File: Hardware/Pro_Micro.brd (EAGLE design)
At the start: 17.8 x 33 mm, 33 parts, among them U2 MIC5219, U3 ATMEGA32U4, X1 USB-MICROB, Y1 16MHz

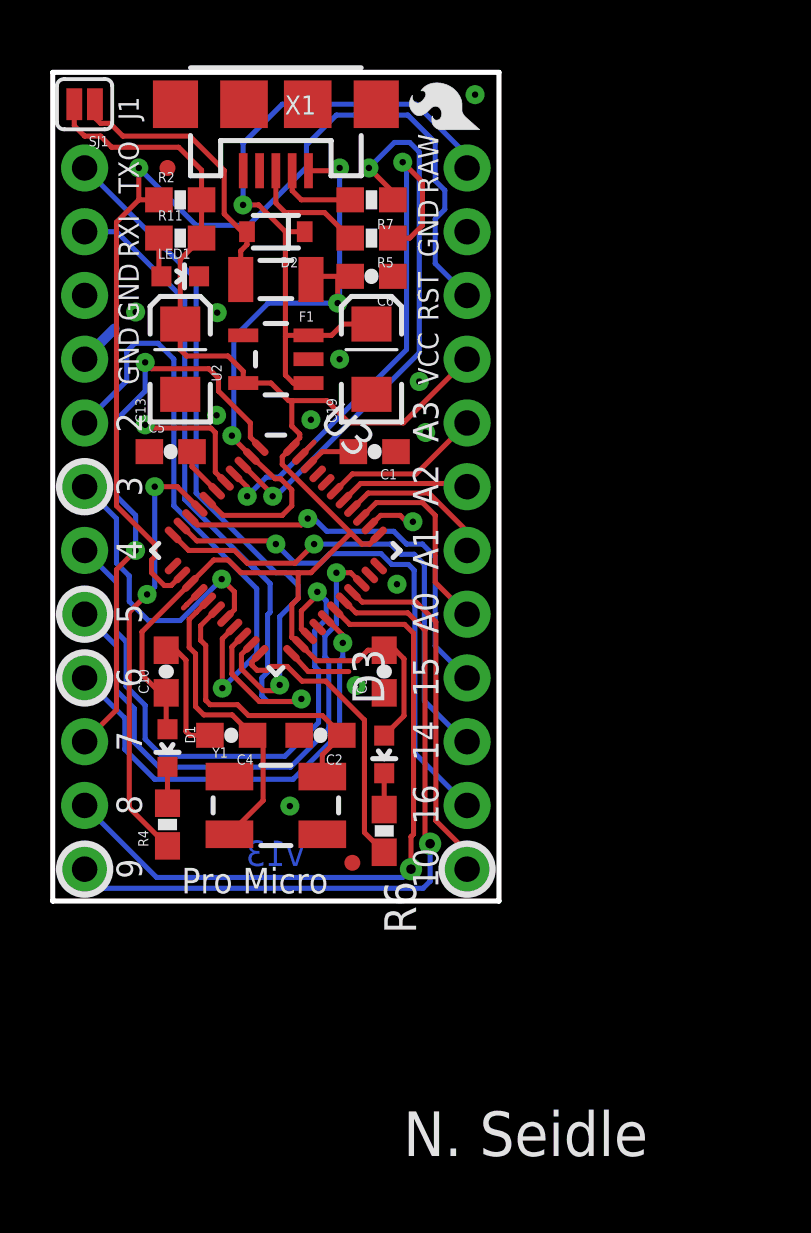
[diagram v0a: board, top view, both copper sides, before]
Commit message: Updated v13 design files
Updated usb connector, IC footprint and route job and moved from 0402 to
0603.
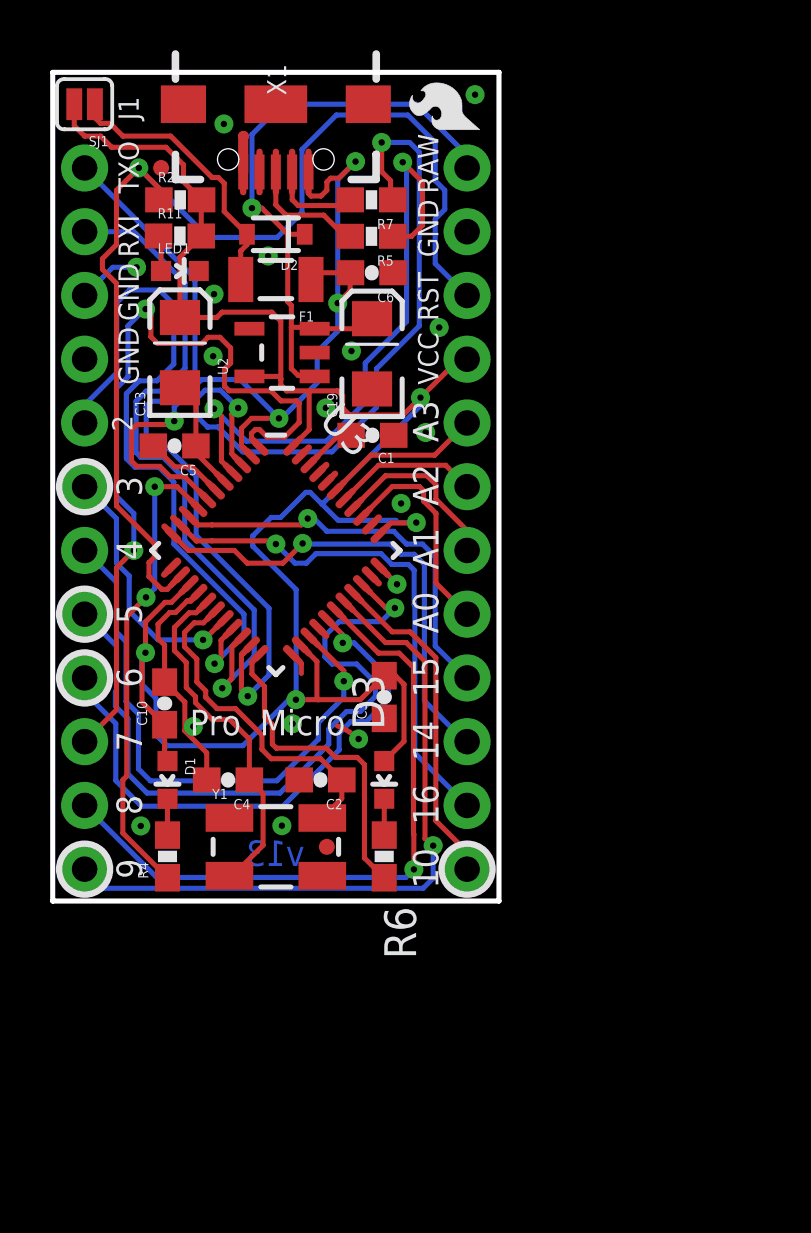
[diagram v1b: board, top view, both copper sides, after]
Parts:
- removed U$5: CREATIVE_COMMONS, SparkFun:CREATIVE_COMMONS
- added FRAME1: FRAME-LETTER, SparkFun-Aesthetics:CREATIVE_COMMONS
- U3: device Testing:QFN-44-NOPAD_1:1 -> Testing:QFN-44-NOPAD_1:1-OUTFAKES
- X1: value USB-MICROB -> (none); device SparkFun-Connectors:USB-MICROB -> Testing:USB-AB-MICRO-SMD-V03-IN&OUT
- moved C4 1.78 mm to (6.99, 4.83)
- moved C2 1.78 mm to (10.7, 4.83)
- moved Y1 1.65 mm to (8.89, 2.16)
- moved C10 1.27 mm to (4.46, 7.87)
- moved D1 1.27 mm to (4.57, 4.83)
- moved R4 1.27 mm to (4.57, 1.78)
- moved JP1 1.20 mm to (10.9, 2.16)
- moved C3 1.02 mm to (13.2, 8.13)
- moved D3 1.02 mm to (13.2, 4.83)
- moved R6 1.02 mm to (13.2, 1.78)
- moved C1 0.66 mm to (12.7, 18.6)
- moved U2 0.36 mm to (9.14, 21.9)
- moved C5 0.28 mm to (4.85, 18.1), turned to 180 degrees
- moved C13 0.26 mm to (5.07, 21.9)
- moved JP2 0.25 mm to (4.32, 29.2)
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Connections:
- net GND: now also X1.GND1; no longer X1.GND, X1.MT1, X1.MT2, X1.MT3, X1.MT4
- net N$6: now also X1.D-1; no longer X1.D-
- net N$8: now also X1.D+1; no longer X1.D+
- net UVCC: now also X1.VBUS1; no longer X1.VBUS
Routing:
- net VCC: track 62.4 -> 83.7 mm, vias 0 -> 4
- net D7: track 23.4 -> 32.8 mm
- net UVCC: track 26.2 -> 33.6 mm, vias 3 -> 4
- net D-: track 22.2 -> 28.7 mm
- net D5: track 22.4 -> 27.6 mm
- net D6: track 18.5 -> 23.2 mm
- net D2: track 23.5 -> 27.8 mm
- net D+: track 21.6 -> 24.6 mm
- net RESET: track 42.1 -> 44.6 mm
- net GND: track 17.9 -> 20.0 mm, vias 13 -> 17
- net D3: track 11.9 -> 9.86 mm
- net RXI: track 29.1 -> 27.1 mm
- net D4: track 24.0 -> 22.3 mm
- net N$1: track 12.3 -> 13.7 mm
- net N$4: track 1.98 -> 3.28 mm
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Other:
- board text added: "Micro"
- board text added: "N. Seidle, revised by P. Lewis"
- board text added: "Pro"
- board text removed: "N. Seidle"
- board text removed: "Pro Micro"
